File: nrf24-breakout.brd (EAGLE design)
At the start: 11.4 x 17.8 mm, 4 parts, among them U1 NRF24

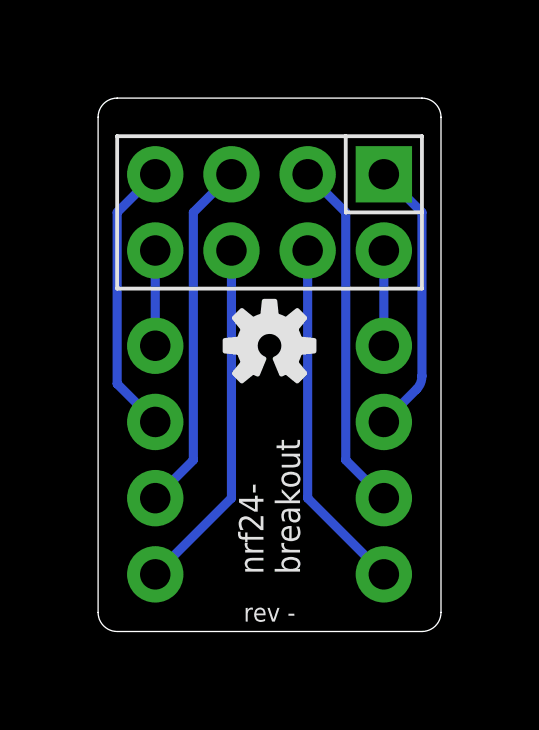
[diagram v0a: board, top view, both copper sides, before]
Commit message: added ground plane, widened vcc trace
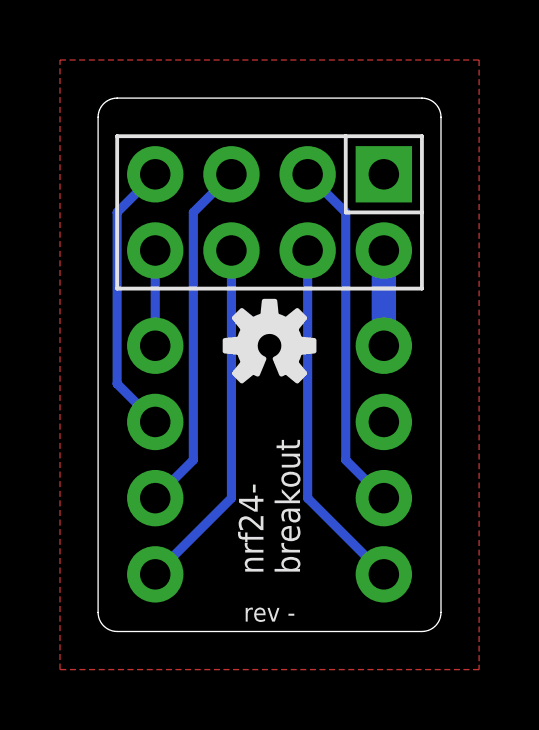
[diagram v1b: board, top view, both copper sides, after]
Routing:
- net GND: track 9.27 -> 0.00 mm
- added copper zone on layer 1, net GND
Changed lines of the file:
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@@
 <contactref element="U1" pad="2"/>
 <contactref element="JP2" pad="1"/>
-<wire x1="9.525" y1="12.7" x2="9.525" y2="9.525" width="0.3048" layer="16"/>
+<wire x1="9.525" y1="12.7" x2="9.525" y2="9.525" width="0.8128" layer="16"/>
 </signal>
 <signal name="GND">
 <contactref element="U1" pad="1"/>
 <contactref element="JP2" pad="2"/>
-<wire x1="9.525" y1="15.24" x2="10.795" y2="13.97" width="0.3048" layer="16"/>
-<wire x1="10.795" y1="13.97" x2="10.795" y2="8.518025" width="0.3048" layer="16"/>
-<wire x1="10.795" y1="8.518025" x2="10.6090125" y2="8.0690125" width="0.3048" layer="16" curve="-45"/>
-<wire x1="10.6090125" y1="8.0690125" x2="9.525" y2="6.985" width="0.3048" layer="16"/>
+<polygon width="0.3048" layer="1">
+<vertex x="-1.27" y="19.05"/>
+<vertex x="12.7" y="19.05"/>
+<vertex x="12.7" y="-1.27"/>
+<vertex x="-1.27" y="-1.27"/>
+</polygon>
 </signal>
 <signal name="CE">

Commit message: small aesthetic changes
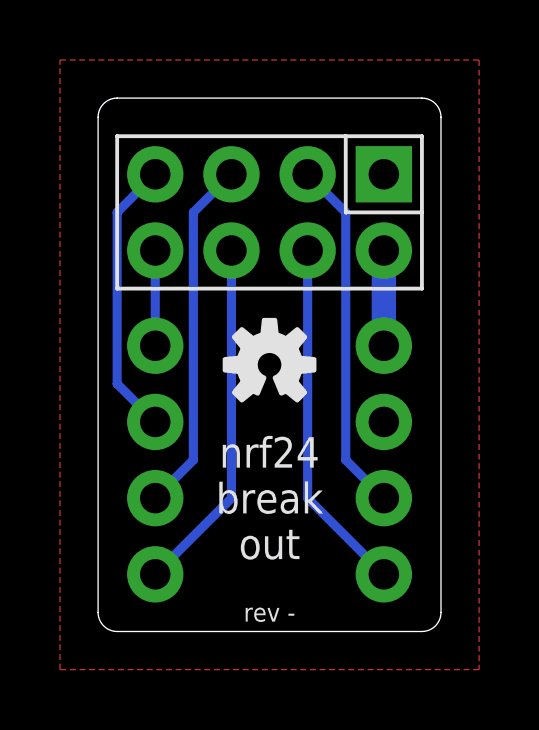
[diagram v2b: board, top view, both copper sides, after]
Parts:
- moved LOGO1 0.63 mm to (5.71, 8.89)
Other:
- board text added: "nrf24 break out"
- board text removed: "nrf24- breakout"
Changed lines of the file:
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@@
 <text x="3.175" y="6.985" size="0.6096" layer="22" font="vector" rot="MR0" align="center-right">MISO</text>
 <text x="3.175" y="9.525" size="0.6096" layer="22" font="vector" rot="MR0" align="center-right">IRQ</text>
-<text x="5.715" y="1.905" size="0.8128" layer="21" font="vector" rot="R90" align="center-left">nrf24-
-breakout</text>
+<text x="5.715" y="4.445" size="1.016" layer="21" font="vector" ratio="15" rot="R180" align="center">nrf24
+break
+out</text>
 <text x="5.715" y="0.635" size="0.6096" layer="21" font="vector" rot="R180" align="center">rev -</text>
 <wire x1="0.635" y1="16.51" x2="8.255" y2="16.51" width="0.3048" layer="22"/>
@@
 </autorouter>
 <elements>
-<element name="U1" library="nrf24" package="NRF24" value="NRF24" x="5.715" y="13.97" smashed="yes"/>
+<element name="U1" library="nrf24" package="NRF24" value="NRF24" x="5.715" y="13.97" smashed="yes">
+<attribute name="PN" value="M20-7830446" x="5.715" y="13.97" size="1.778" layer="27" display="off"/>
+</element>
 <element name="JP1" library="SparkFun-Connectors" package="1X04_NO_SILK_ALL_ROUND" value="" x="1.905" y="9.525" smashed="yes" rot="R270">
 <attribute name="VALUE" x="-1.27" y="10.795" size="1.27" layer="27" rot="R270"/>
+<attribute name="PN" value="M20-9990446" x="1.905" y="9.525" size="1.778" layer="27" rot="R270" display="off"/>
 </element>
 <element name="JP2" library="SparkFun-Connectors" package="1X04_NO_SILK_ALL_ROUND" value="" x="9.525" y="9.525" smashed="yes" rot="R270">
 <attribute name="VALUE" x="6.35" y="10.795" size="1.27" layer="27" rot="R270"/>
+<attribute name="PN" value="M20-9990446" x="9.525" y="9.525" size="1.778" layer="27" rot="R270" display="off"/>
 </element>
-<element name="LOGO1" library="SparkFun-Aesthetics" package="OSHW-LOGO-S" value="OSHW-LOGOS" x="5.715" y="9.525"/>
+<element name="LOGO1" library="SparkFun-Aesthetics" package="OSHW-LOGO-S" value="OSHW-LOGOS" x="5.715" y="8.89"/>
 </elements>
 <signals>
